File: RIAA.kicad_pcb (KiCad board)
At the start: 2 copper layers, 112 x 202 mm, 65 parts, among them K1 G6K-2, P10 From Keyboard, P8 From main PCB, P9 From Wire, Q1 Q_NPN_BCE, U5 OPA2134, U6 OPA2134, U7 LM317_TO-220

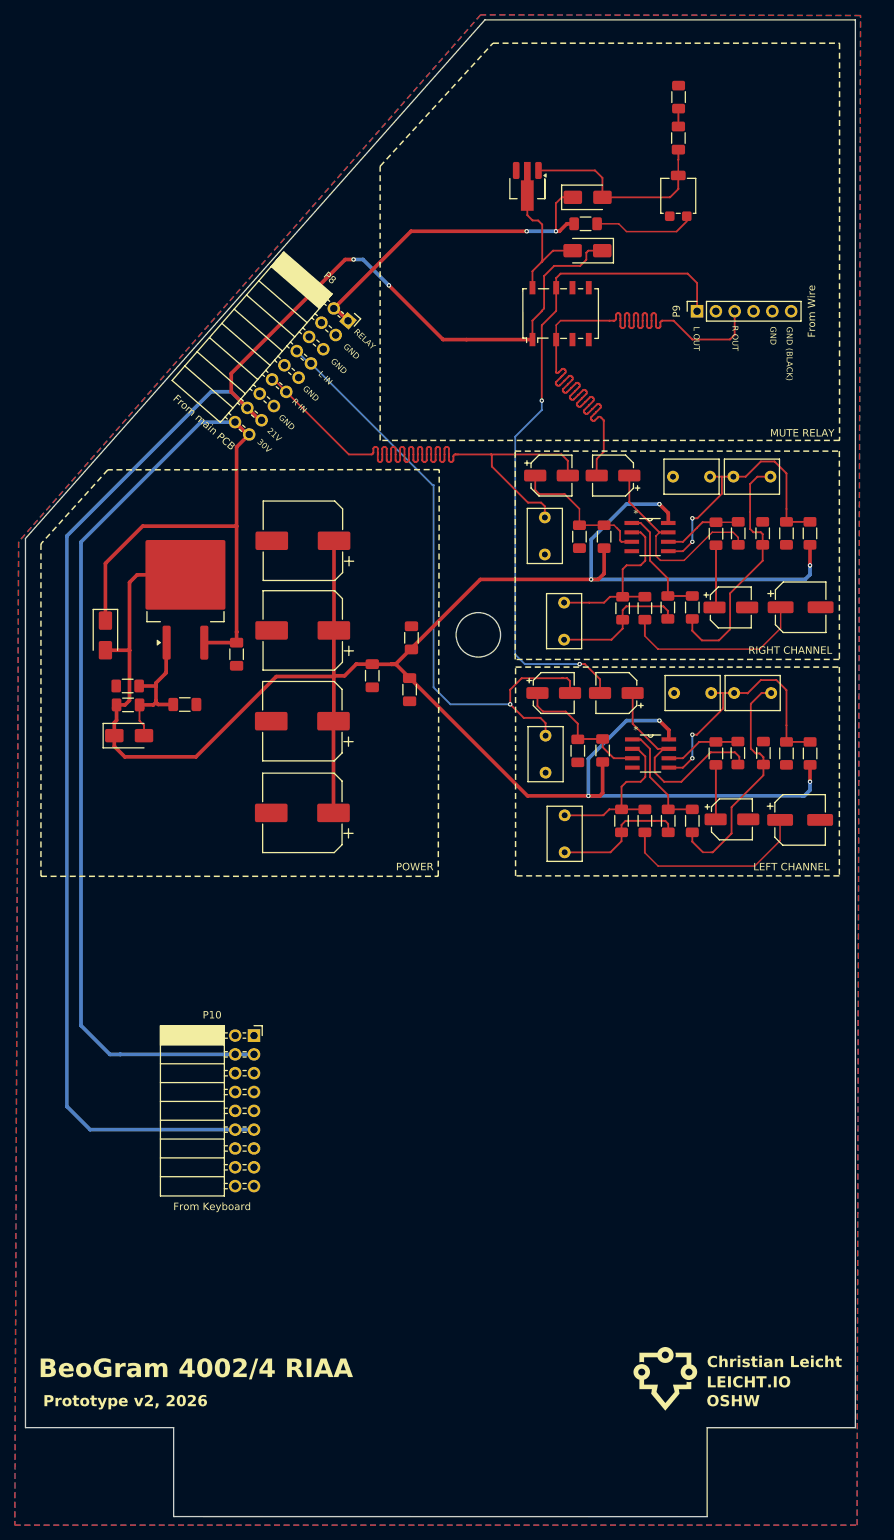
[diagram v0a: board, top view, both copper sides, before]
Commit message: Added RIAA response and optimized layout.
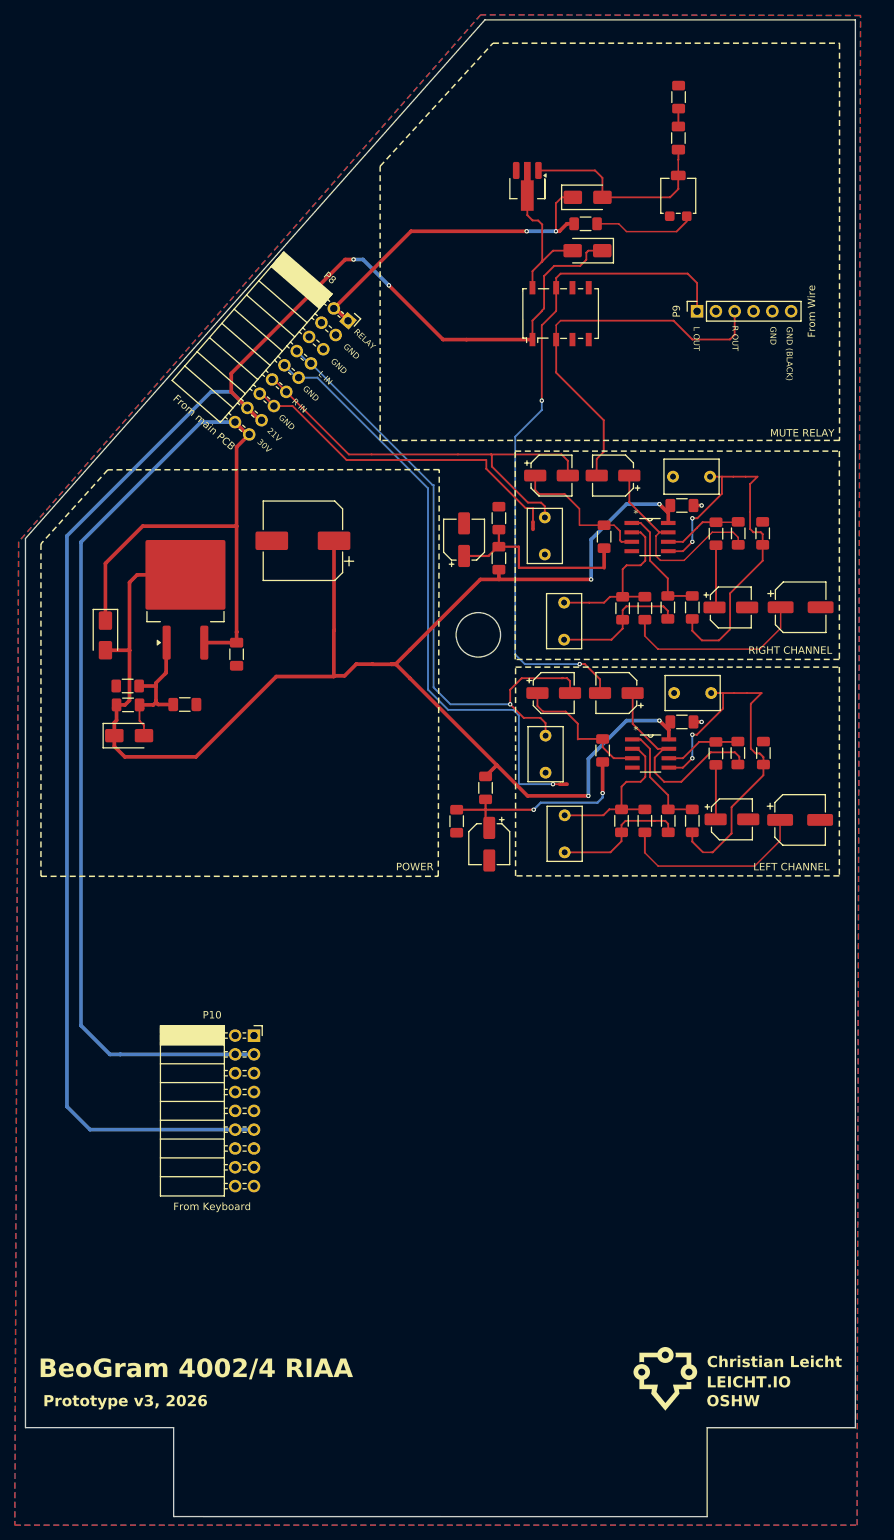
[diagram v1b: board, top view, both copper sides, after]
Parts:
- removed C104, C204: 2uF, Capacitor_THT:C_Rect_L7.2mm_W4.5mm_P5.00mm_FKS2_FKP2_MKS2_MKP2
- removed C2, C3, C31: 470uF, Capacitor_SMD:CP_Elec_10x10.5
- removed C32: 100nF, Capacitor_SMD:C_1206_3216Metric_Pad1.33x1.80mm_HandSolder
- removed R102, R111, R112, R202, R211, R212: 47k, Resistor_SMD:R_1206_3216Metric_Pad1.30x1.75mm_HandSolder
- added C34: 10uF, Capacitor_SMD:CP_Elec_5x5.4, F.Cu at (205.0, 138.6)
- added C35: 10uF, Capacitor_SMD:CP_Elec_5x5.4, F.Cu at (201.6, 97.5)
- added NT1: NetTie_2, NetTie:NetTie-2_SMD_Pad0.5mm, F.Cu at (215.0, 130.5)
- added NT2: NetTie_2, NetTie:NetTie-2_SMD_Pad0.5mm, F.Cu at (210.9, 95.6)
- added R23: 100k, Resistor_SMD:R_1206_3216Metric_Pad1.30x1.75mm_HandSolder, F.Cu at (204.5, 131.0)
- added R24: 100k, Resistor_SMD:R_1206_3216Metric_Pad1.30x1.75mm_HandSolder, F.Cu at (200.6, 135.5)
- added R25: 100k, Resistor_SMD:R_1206_3216Metric_Pad1.30x1.75mm_HandSolder, F.Cu at (206.3, 100.0)
- added R26: 100k, Resistor_SMD:R_1206_3216Metric_Pad1.30x1.75mm_HandSolder, F.Cu at (206.3, 94.6)
- C102, C202: value 39nF -> 33nF
- C103, C203: value 200uF -> 220uF
- Q1: value Q_NPN_BCE -> BCV49
- R104, R204: value 499 -> 590
- R105, R205: value 80.6k -> 95.3k
- R106, R206: value 8.45k -> 10k
- R19: value 5k6 -> 4k7
- moved C28 40.6 mm to (231.0, 92.9), turned to 180 degrees
- moved C27 37.0 mm to (231.0, 122.1), turned to 180 degrees
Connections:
- P8 pad 10: GND -> GND L IN PICKUP
- P8 pad 13: GND -> GND R IN PICKUP
- P8 pad 14: GND -> GND R IN PICKUP
- P8 pad 9: GND -> GND L IN PICKUP
- R103 pad 1: 24VDC+ -> VREF_L
- R107 pad 1: Net-(C104-Pad1) -> Net-(U5B-+)
- R108 pad 1: Net-(C104-Pad1) -> Net-(U5B-+)
- R203 pad 1: 24VDC+ -> VREF_R
- R207 pad 1: Net-(C204-Pad1) -> Net-(U6B-+)
- R208 pad 1: Net-(C204-Pad1) -> Net-(U6B-+)
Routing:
- net 24VDC+: track 304.7 -> 210.5 mm, vias 6 -> 4
- net GND L IN PICKUP: track 0.00 -> 81.9 mm, vias 0 -> 1
- net GND R IN PICKUP: track 0.00 -> 45.8 mm
- net R OUT: track 93.5 -> 52.2 mm
- net Net-(C204-Pad1): track 33.7 -> 0.00 mm
- net Net-(C104-Pad1): track 31.9 -> 0.00 mm
- net R IN PICKUP: track 91.0 -> 59.2 mm
- net VREF_L: track 0.00 -> 27.8 mm, vias 0 -> 2
- net VREF_R: track 0.00 -> 26.3 mm
- net Net-(U6B-+): track 36.2 -> 53.0 mm
- net Net-(U5B-+): track 36.3 -> 51.9 mm
- net GND: track 0.00 -> 2.20 mm, vias 0 -> 2
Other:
- board text added: "Prototype v3, 2026"
- board text removed: "Prototype v2, 2026"
